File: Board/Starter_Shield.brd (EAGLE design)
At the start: 68.6 x 53.3 mm, 12 parts

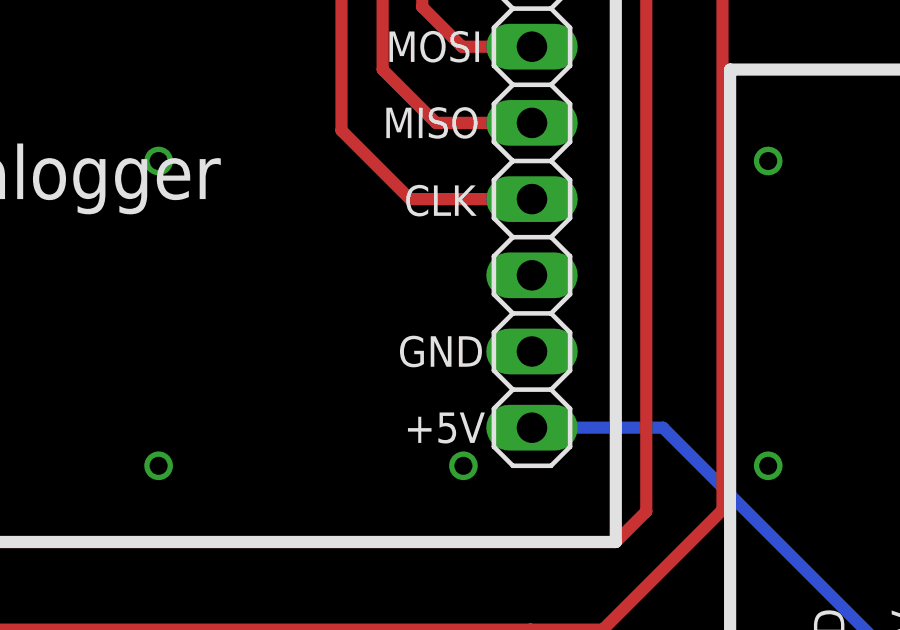
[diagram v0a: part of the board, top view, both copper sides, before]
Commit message: updated gnd on the datalogger to the right pin - V1.2 now
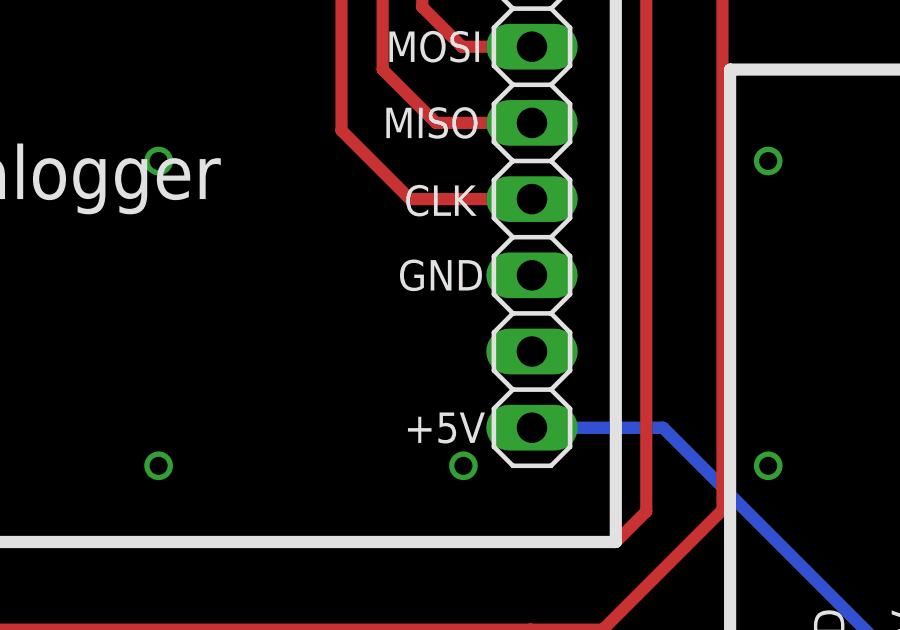
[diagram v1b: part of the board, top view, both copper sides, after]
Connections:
- net GND: now also DATA.6; no longer DATA.7
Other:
- board text added: "V 1.2 8-2019"
- board text removed: "V 1.1 1-2019"
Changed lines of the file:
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@@
 <wire x1="1.016" y1="53.34" x2="64.516" y2="53.34" width="0.254" layer="20"/>
 <text x="67.31" y="11.43" size="1.778" layer="21" font="vector" rot="R90">Starter Shield</text>
-<text x="60.96" y="15.24" size="1.016" layer="22" font="vector" rot="MR90">V 1.1 1-2019</text>
+<text x="60.96" y="15.24" size="1.016" layer="22" font="vector" rot="MR90">V 1.2 8-2019</text>
 <text x="58.42" y="15.24" size="1.016" layer="22" font="vector" rot="MR90">T. Boyle</text>
 <text x="55.88" y="15.24" size="1.016" layer="22" font="vector" rot="MR90">B. Weinberg</text>
@@
 <text x="18.1864" y="14.478" size="1.778" layer="21" font="vector" rot="R270">LED</text>
 <text x="45.72" y="13.97" size="1.016" layer="21" font="vector" rot="R90">GND</text>
-<text x="30.8356" y="24.892" size="1.016" layer="21" font="vector">GND</text>
+<text x="30.8356" y="27.432" size="1.016" layer="21" font="vector">GND</text>
 <text x="29.3116" y="9.0424" size="1.016" layer="21" font="vector" rot="R180">GND</text>
 <text x="24.4348" y="11.7348" size="1.016" layer="21" font="vector" rot="R90">GND</text>
@@
 <contactref element="TEMP" pad="1"/>
 <contactref element="POWER" pad="7"/>
-<contactref element="DATA" pad="7"/>
 <polygon width="0.4064" layer="1">
 <vertex x="69.85" y="58.42"/>
@@
 <via x="63.5" y="11.43" extent="1-16" drill="0.6"/>
 <via x="43.18" y="31.75" extent="1-16" drill="0.6"/>
+<contactref element="DATA" pad="6"/>
 </signal>
 <signal name="N$13">
